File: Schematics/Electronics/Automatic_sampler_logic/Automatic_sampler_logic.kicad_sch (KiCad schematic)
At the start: 14 parts, among them J1 MOT_X_SOCK, J2 MOT_Y_SOCK, J3 MOT_Z_SOCK, J4 Jack-DC, J5 FINAL_SOCK, J6 LCD_SOCK, J7 POWER_SOCK, J8 BUTTON_SOCK, U1 DRV8825, U2 DRV8825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

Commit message: Changed schematics
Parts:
- removed J4: Jack-DC, Connector_BarrelJack:BarrelJack_Horizontal, symbol Connector:Jack-DC
- removed U1, U2, U3: DRV8825, symbol ATSS_Library:DRV8825
- added A2, A3, A4: Pololu_Breakout_DRV8825, Module:Pololu_Breakout-16_15.2x20.3mm, symbol Driver_Motor:Pololu_Breakout_DRV8825
- added J4: Power, Connector_PinSocket_2.54mm:PinSocket_1x02_P2.54mm_Vertical, symbol Connector_Generic:Conn_01x02
- added J9: MOT_X_SOCK2, Connector_PinSocket_2.54mm:PinSocket_1x05_P2.54mm_Vertical, symbol Connector:Conn_01x05_Socket
- J8: footprint (none) -> Connector_PinSocket_2.54mm:PinSocket_1x01_P2.54mm_Vertical
- U5: footprint (none) -> Package_TO_SOT_THT:TO-220-3_Vertical
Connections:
- net +12V: now also A2.8 (VMOT), A3.8 (VMOT), A4.8 (VMOT), J4.2 (Pin_2)
- net +5V: now also A2.13 (~{RST}), A2.14 (~{SLP}), A3.13 (~{RST}), A3.14 (~{SLP}), A4.13 (~{RST}), A4.14 (~{SLP})
- net F_Y: no longer J5.3 (Pin_3)
- net F_Z: now also J5.3 (Pin_3)
- net GND: now also A2.1 (GND), A2.7 (GND), A3.1 (GND), A3.7 (GND), A4.1 (GND), A4.7 (GND), J4.1 (Pin_1)
- net MOT_DIR: now also A2.16 (DIR), A3.16 (DIR), A4.16 (DIR)
- net MOT_EN_X: now also A2.9 (~{EN})
- net MOT_EN_Y: now also A3.9 (~{EN})
- net MOT_EN_Z: now also A4.9 (~{EN})
- net MOT_ST: now also A2.15 (STEP), A3.15 (STEP), A4.15 (STEP)
- net at J1.5 (Pin_5): now also A2.2 (~{FLT}), J9.5 (Pin_5)
- net at J1.2 (Pin_2): now also A2.5 (B1), J9.2 (Pin_2)
- net at J1.4 (Pin_4): now also A2.3 (A2), J9.4 (Pin_4)
- net at J1.3 (Pin_3): now also A2.4 (A1), J9.3 (Pin_3)
- net at J1.1 (Pin_1): now also A2.6 (B2), J9.1 (Pin_1)
- net at J2.1 (Pin_1): now also A3.6 (B2)
- net at J2.2 (Pin_2): now also A3.5 (B1)
- net at J2.3 (Pin_3): now also A3.4 (A1)
- net at J2.4 (Pin_4): now also A3.3 (A2)
- net at J2.5 (Pin_5): now also A3.2 (~{FLT})
- net at J3.5 (Pin_5): now also A4.2 (~{FLT})
- net at J3.2 (Pin_2): now also A4.5 (B1)
- net at J3.4 (Pin_4): now also A4.3 (A2)
- net at J3.3 (Pin_3): now also A4.4 (A1)
- net at J3.1 (Pin_1): now also A4.6 (B2)
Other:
- moved on the sheet: J1, J2, J3

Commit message: Correcting errors
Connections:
- net MOT_EN_X: now also U4.12 (GPIO9); no longer U4.9 (GPIO6)
- net MOT_EN_Z: now also U4.9 (GPIO6); no longer U4.12 (GPIO9)
- net at A2.6 (B2), J1.1 (Pin_1): no longer J9.1 (Pin_1)
- net at A2.5 (B1), J1.2 (Pin_2): no longer J9.2 (Pin_2)
- net at A2.4 (A1), J1.3 (Pin_3): no longer J9.3 (Pin_3)
- net at A2.3 (A2), J1.4 (Pin_4): no longer J9.4 (Pin_4)
- net at A2.2 (~{FLT}), J1.5 (Pin_5): no longer J9.5 (Pin_5)

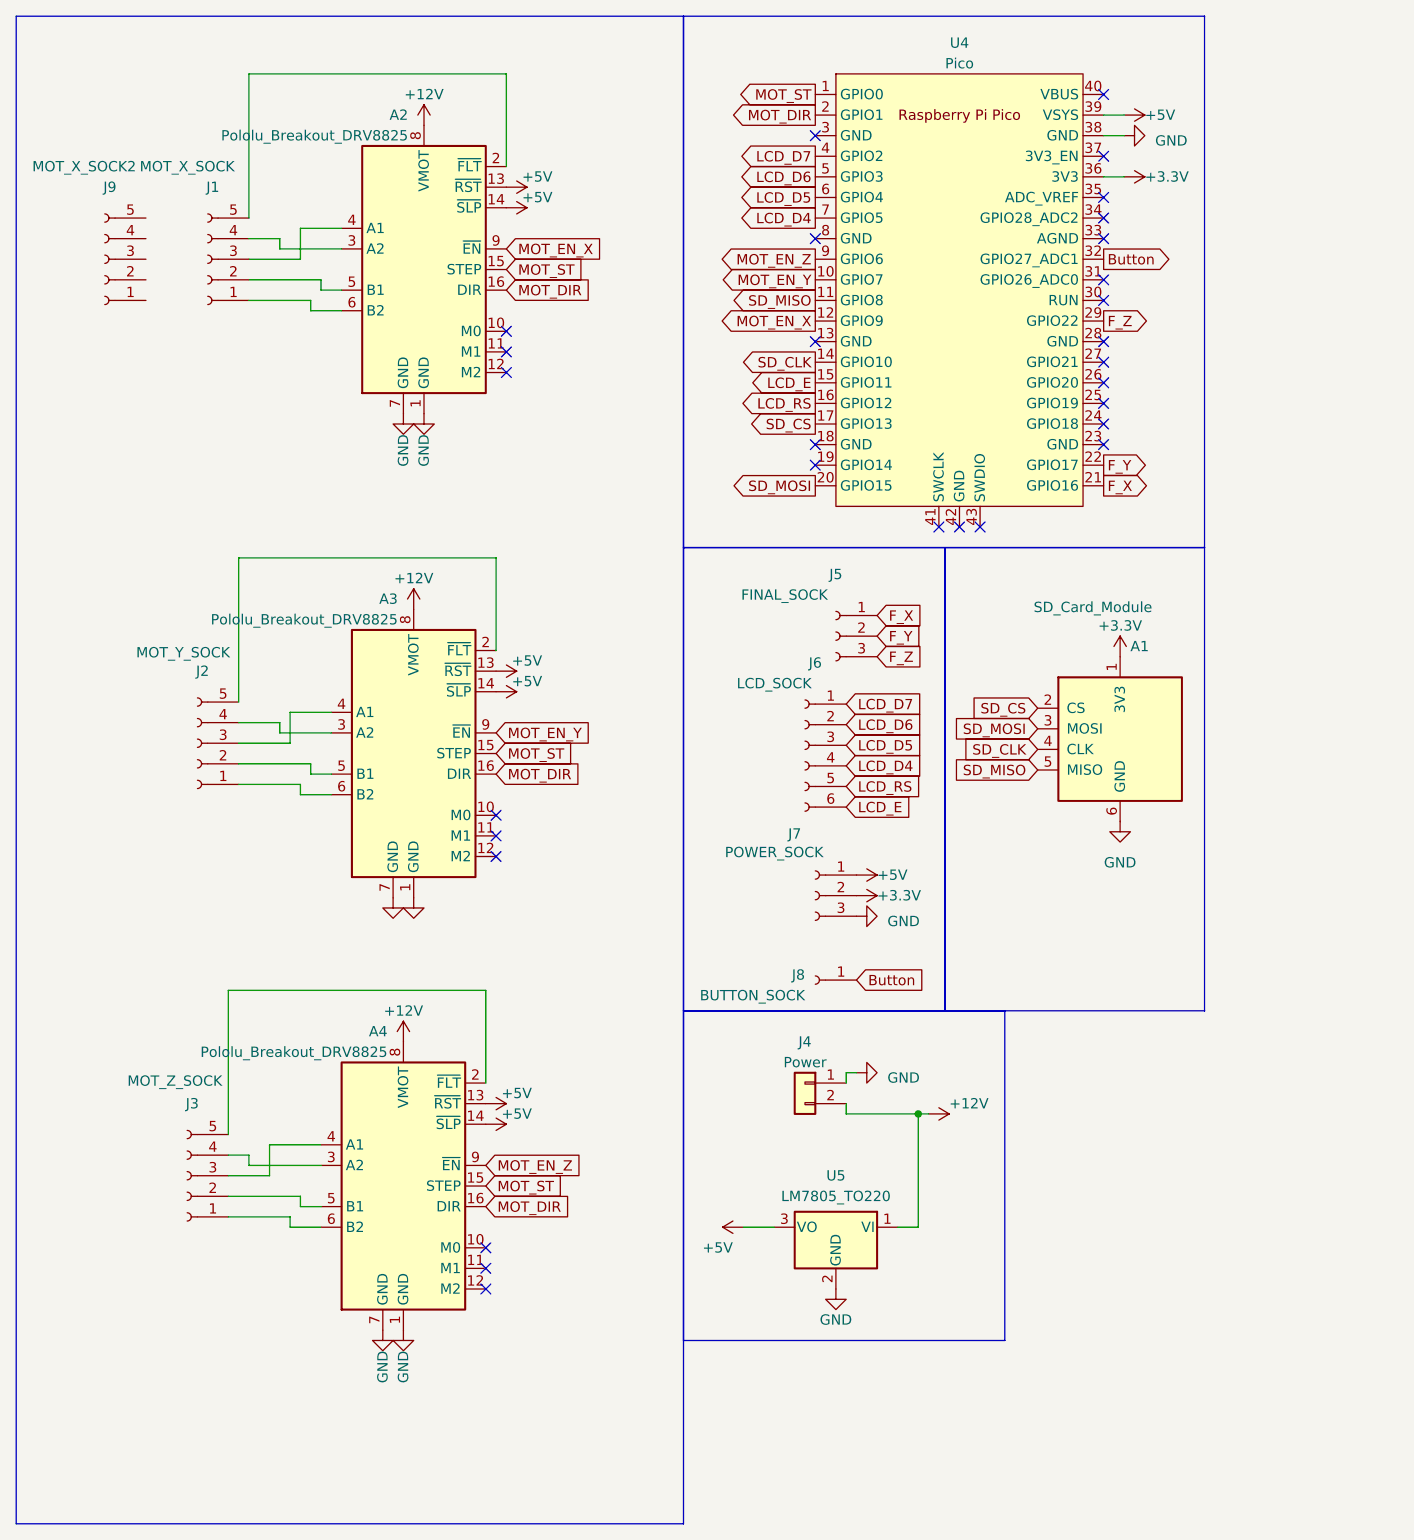
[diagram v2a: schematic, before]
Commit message: Major circuit changes
Removed from the circuit and the firmware the LCD and the SD card. They will be substituted by serial communication.
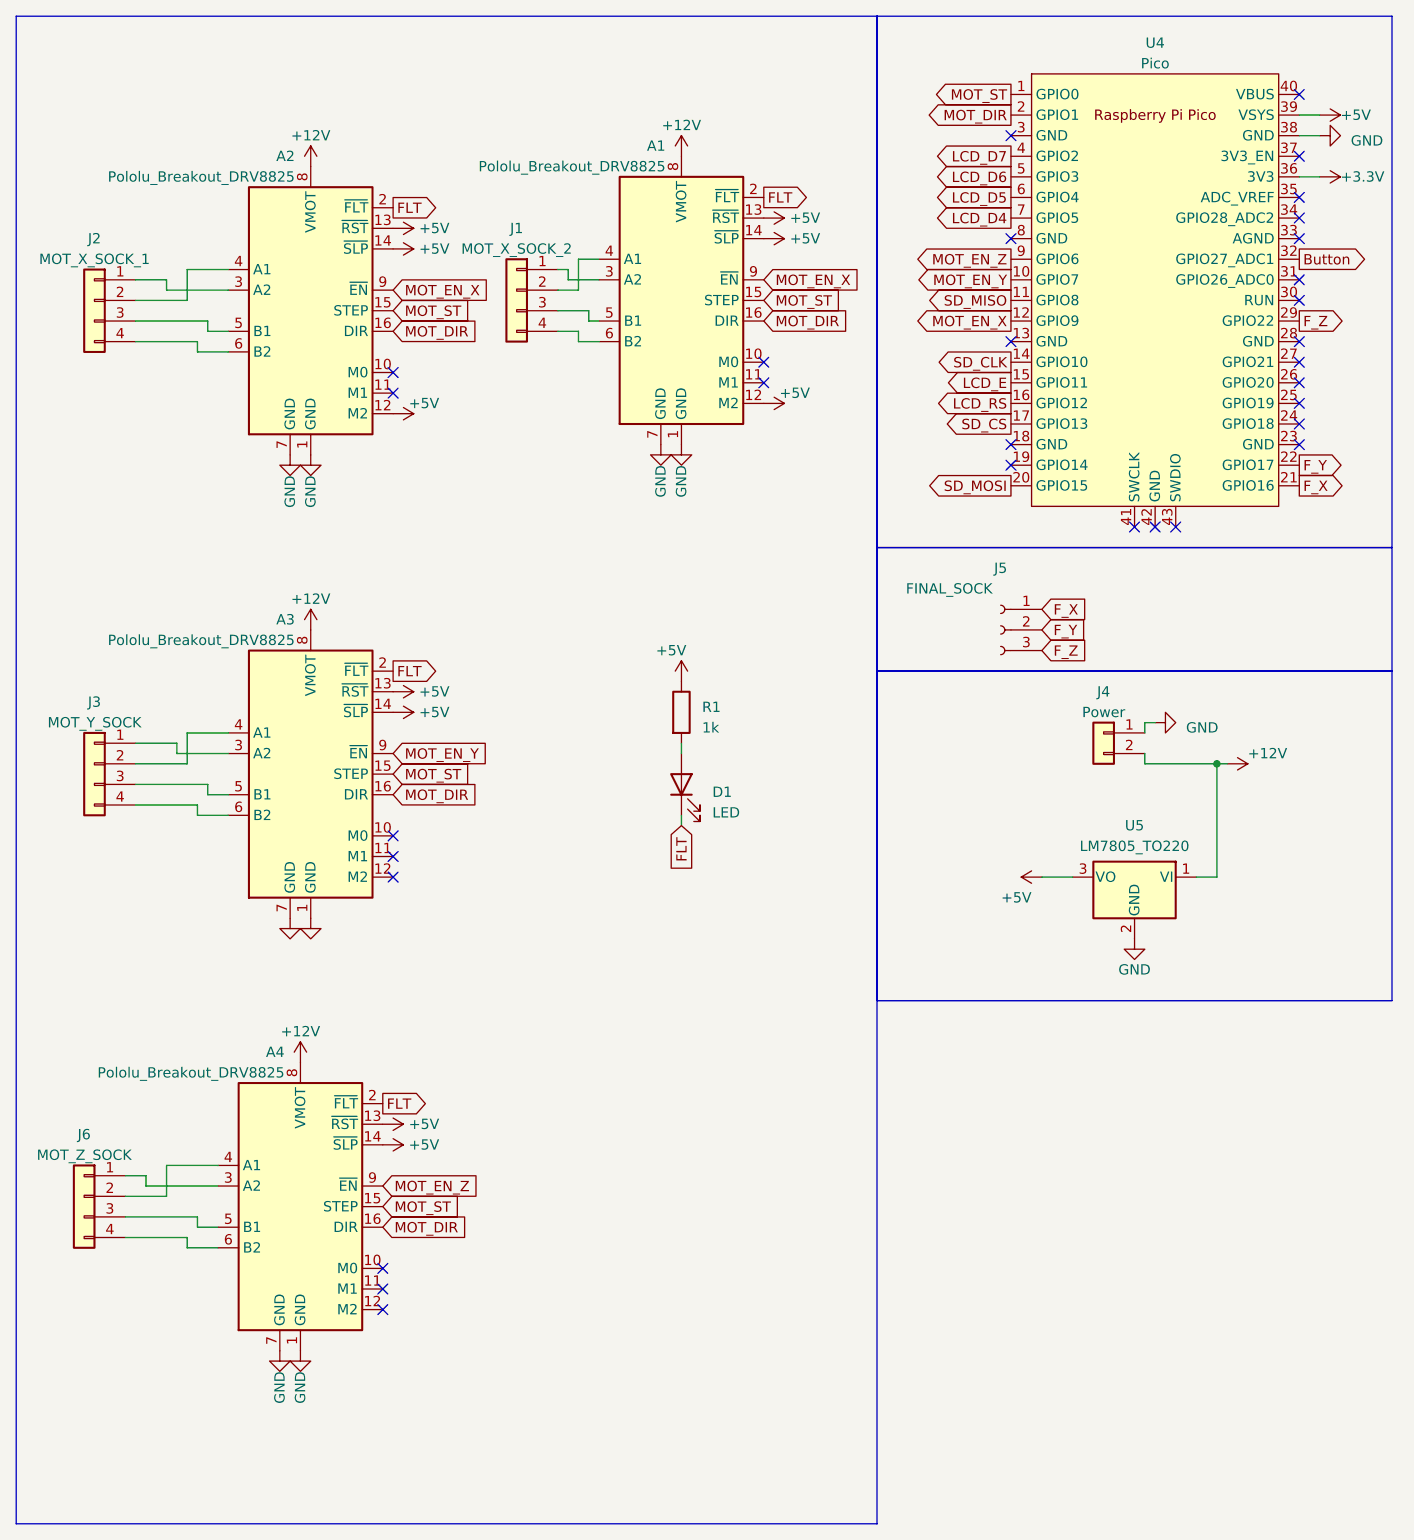
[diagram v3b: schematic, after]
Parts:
- removed A1: SD_Card_Module, Arduino_Peripherals:SD_Card_Module, symbol Arduino_Peripherals:SD_Card_Module
- removed J1: MOT_X_SOCK, Connector_PinSocket_2.54mm:PinSocket_1x05_P2.54mm_Vertical, symbol Connector:Conn_01x05_Socket
- removed J2: MOT_Y_SOCK, Connector_PinSocket_2.54mm:PinSocket_1x05_P2.54mm_Vertical, symbol Connector:Conn_01x05_Socket
- removed J3: MOT_Z_SOCK, Connector_PinSocket_2.54mm:PinSocket_1x05_P2.54mm_Vertical, symbol Connector:Conn_01x05_Socket
- removed J6: LCD_SOCK, Connector_PinSocket_2.54mm:PinSocket_1x06_P2.54mm_Vertical, symbol Connector:Conn_01x06_Socket
- removed J7: POWER_SOCK, Connector_PinSocket_2.54mm:PinSocket_1x03_P2.54mm_Vertical, symbol Connector:Conn_01x03_Socket
- removed J8: BUTTON_SOCK, Connector_PinSocket_2.54mm:PinSocket_1x01_P2.54mm_Vertical, symbol Connector:Conn_01x01_Socket
- removed J9: MOT_X_SOCK2, Connector_PinSocket_2.54mm:PinSocket_1x05_P2.54mm_Vertical, symbol Connector:Conn_01x05_Socket
- added A1: Pololu_Breakout_DRV8825, Module:Pololu_Breakout-16_15.2x20.3mm, symbol Driver_Motor:Pololu_Breakout_DRV8825
- added D1: LED, symbol Device:LED
- added J1: MOT_X_SOCK_2, symbol Connector_Generic:Conn_01x04
- added J2: MOT_X_SOCK_1, symbol Connector_Generic:Conn_01x04
- added J3: MOT_Y_SOCK, symbol Connector_Generic:Conn_01x04
- added J6: MOT_Z_SOCK, symbol Connector_Generic:Conn_01x04
- added R1: 1k, symbol Device:R
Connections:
- net +12V: now also A1.8 (VMOT)
- net +5V: now also A2.12 (M2), A1.12 (M2), A1.13 (~{RST}), A1.14 (~{SLP}), R1.1
- net GND: now also A1.1 (GND), A1.7 (GND)
- net MOT_DIR: now also A1.16 (DIR)
- net MOT_EN_X: now also A1.9 (~{EN})
- net MOT_ST: now also A1.15 (STEP)
- net FLT: now reaches A3.2 (~{FLT})
- net FLT: now also A2.2 (~{FLT}), A4.2 (~{FLT}), A1.2 (~{FLT}), D1.1 (K)
- net at A3.3 (A2): now also J3.1 (Pin_1)
- net at A3.4 (A1): now also J3.2 (Pin_2)
- net at A3.5 (B1): now also J3.3 (Pin_3)
- net at A3.6 (B2): now also J3.4 (Pin_4)
- net at A4.3 (A2): now also J6.1 (Pin_1)
- net at A4.4 (A1): now also J6.2 (Pin_2)
- net at A4.5 (B1): now also J6.3 (Pin_3)
- net at A4.6 (B2): now also J6.4 (Pin_4)
- net at A2.6 (B2): now also J2.4 (Pin_4)
- net at A2.5 (B1): now also J2.3 (Pin_3)
- net at A2.4 (A1): now also J2.2 (Pin_2)
- net at A2.3 (A2): now also J2.1 (Pin_1)
- new net: D1.2 (A), R1.2
- new net: A1.3 (A2), J1.1 (Pin_1)
- new net: A1.4 (A1), J1.2 (Pin_2)
- new net: A1.5 (B1), J1.3 (Pin_3)
- new net: A1.6 (B2), J1.4 (Pin_4)
- no-connect marks 30 -> 31
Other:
- moved on the sheet: A2, A3, A4, J4, J5, U4, U5

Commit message: Updating schematic
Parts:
- removed J5: FINAL_SOCK, Connector_PinSocket_2.54mm:PinSocket_1x03_P2.54mm_Vertical, symbol Connector:Conn_01x03_Socket
- added C1: 0.33u, symbol Device:C
- added C2: 0.1u, symbol Device:C
- added J5: FinalSock, Connector_PinSocket_2.54mm:PinSocket_1x04_P2.54mm_Vertical, symbol Connector:Conn_01x04_Socket
- D1: footprint (none) -> LED_THT:LED_D5.0mm
- J1, J2, J3, J6: footprint (none) -> Connector_JST:JST_PH_B4B-PH-K_1x04_P2.00mm_Vertical
- R1: footprint (none) -> Resistor_THT:R_Axial_DIN0207_L6.3mm_D2.5mm_P7.62mm_Horizontal
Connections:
- net +12V: now also C1.1
- net +5V: now also C2.1
- net F_X: now also J5.2 (Pin_2)
- net F_Y: now also J5.3 (Pin_3)
- net F_Z: now also J5.4 (Pin_4)
- net GND: now also C1.2, C2.2, J5.1 (Pin_1)

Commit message: Update Automatic_sampler_logic.kicad_sch
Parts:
- C2: footprint (none) -> Capacitor_THT:C_Disc_D6.0mm_W2.5mm_P5.00mm
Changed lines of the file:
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@@
       (effects (font (size 1.27 1.27)) (justify left))
     )
-    (property "Footprint" "" (at 141.9352 125.73 0)
+    (property "Footprint" "Capacitor_THT:C_Disc_D6.0mm_W2.5mm_P5.00mm" (at 141.9352 125.73 0)
       (effects (font (size 1.27 1.27)) hide)
     )

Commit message: Made PCB for AS
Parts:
- C1: footprint (none) -> Capacitor_THT:C_Disc_D6.0mm_W2.5mm_P5.00mm
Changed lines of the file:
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@@
       (effects (font (size 1.27 1.27)) (justify left))
     )
-    (property "Footprint" "" (at 159.7152 125.73 0)
+    (property "Footprint" "Capacitor_THT:C_Disc_D6.0mm_W2.5mm_P5.00mm" (at 159.7152 125.73 0)
       (effects (font (size 1.27 1.27)) hide)
     )
